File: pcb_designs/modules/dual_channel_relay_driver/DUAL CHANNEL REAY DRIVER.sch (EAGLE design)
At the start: 18 parts, among them T1 BC547, T2 BC547

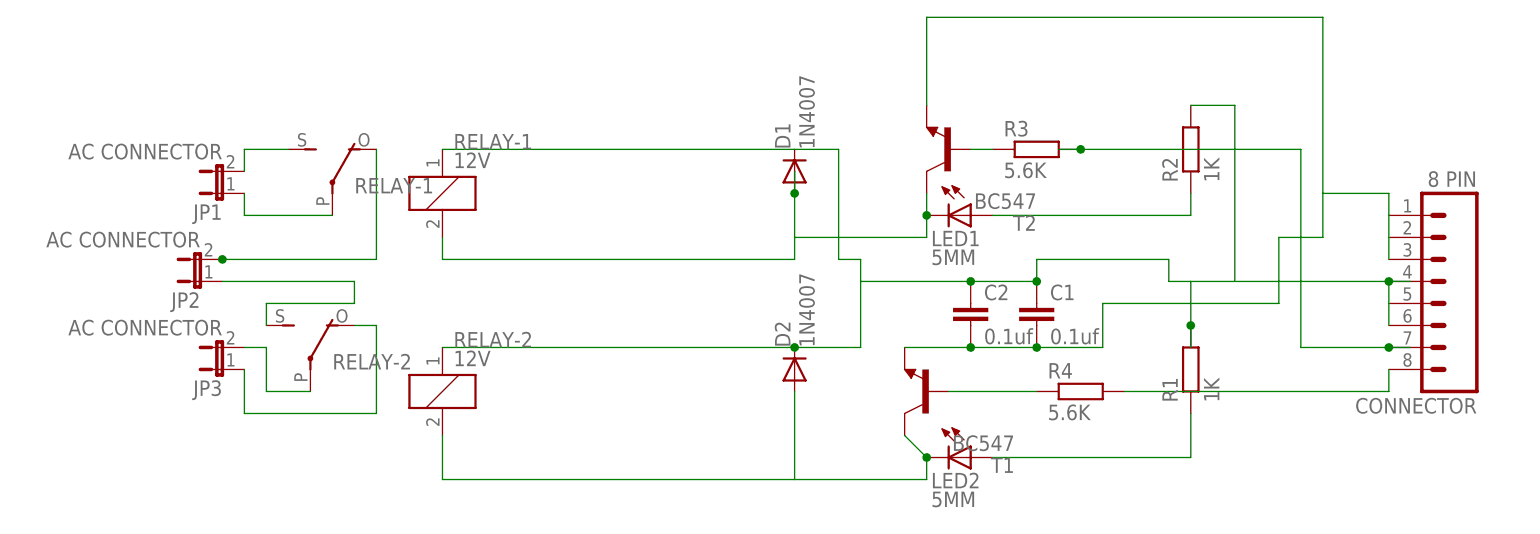
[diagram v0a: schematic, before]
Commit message: 
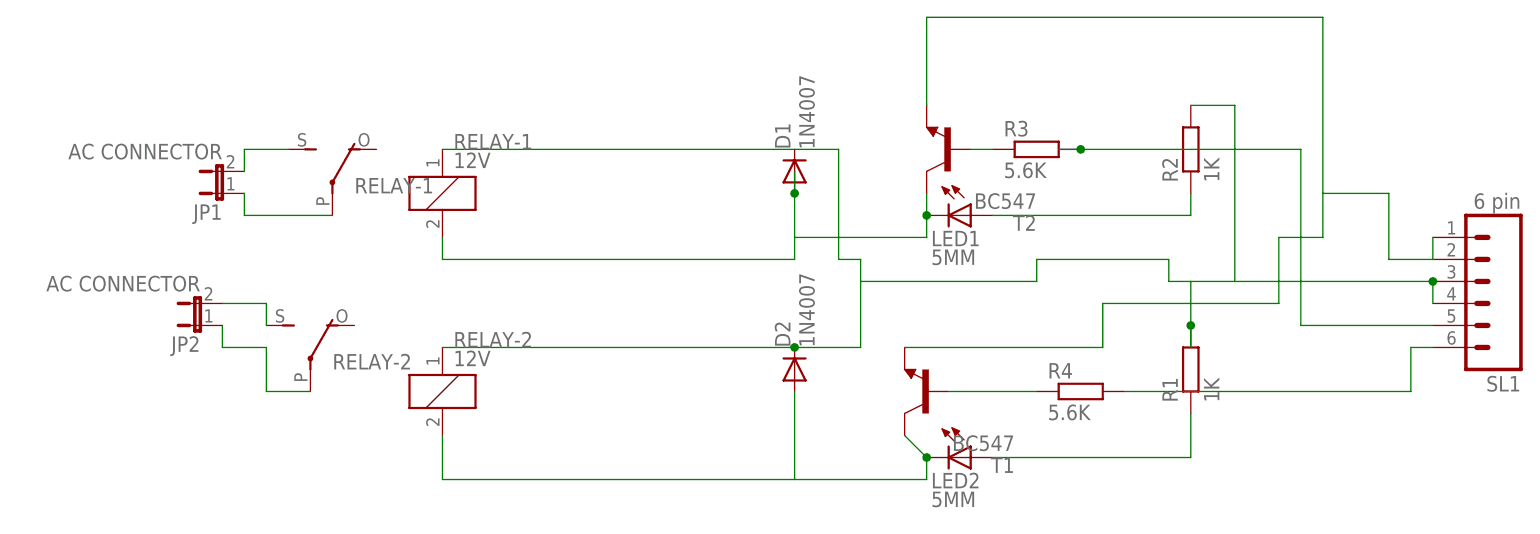
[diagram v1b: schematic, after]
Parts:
- removed C1, C2: 0.1uf, capacitor-wima:C2,5-3
- removed CONNECTOR: 8 PIN, con-amp-quick:M08
- removed JP3: AC CONNECTOR, jumper:JP1E
- added SL1: 6 pin, con-amp-quick:M06
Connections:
- removed net N$11: JP2.2, RELAY-12.O
- removed net N$12: JP2.1, RELAY-22.S
- removed net N$14: JP3.1, RELAY-22.O
- new net N$3: JP2.2, RELAY-22.S
- net N$13: now also JP2.1; no longer JP3.2
- net N$16: now also SL1.1, SL1.2; no longer C1.2, C2.2, CONNECTOR.1, CONNECTOR.2, CONNECTOR.3
- net N$17: now also SL1.5; no longer CONNECTOR.7
- net N$18: now also SL1.6; no longer CONNECTOR.8
- net N$2: now also SL1.3, SL1.4; no longer C1.1, C2.1, CONNECTOR.4, CONNECTOR.5, CONNECTOR.6
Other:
- moved on the sheet: JP2
